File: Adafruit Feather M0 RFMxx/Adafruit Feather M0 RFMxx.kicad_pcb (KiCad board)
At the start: 2 copper layers, 50.8 x 22.9 mm, 50 parts, among them J31 Conn_01x02, J32 Conn_01x02, J33 Conn_01x02, SW1 SPST_TACT-KMR2, U1 2MB Flash, U2 AP2112K-3.3, U3 MCP73831T-2ACI/OT, U31 MCP25625-x-SS, X1 JSTPH, X2 32.768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

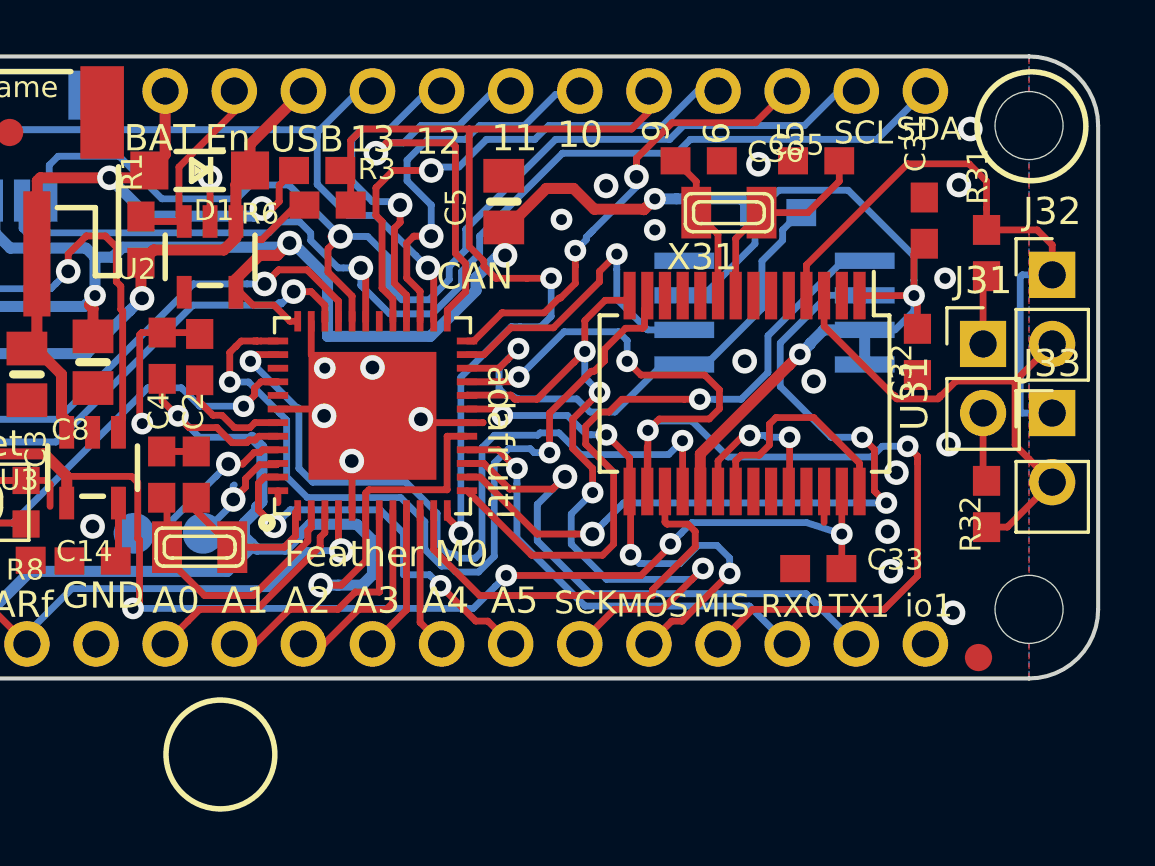
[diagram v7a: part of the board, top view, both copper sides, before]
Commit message: Fix mounting hole. Update silscreen.
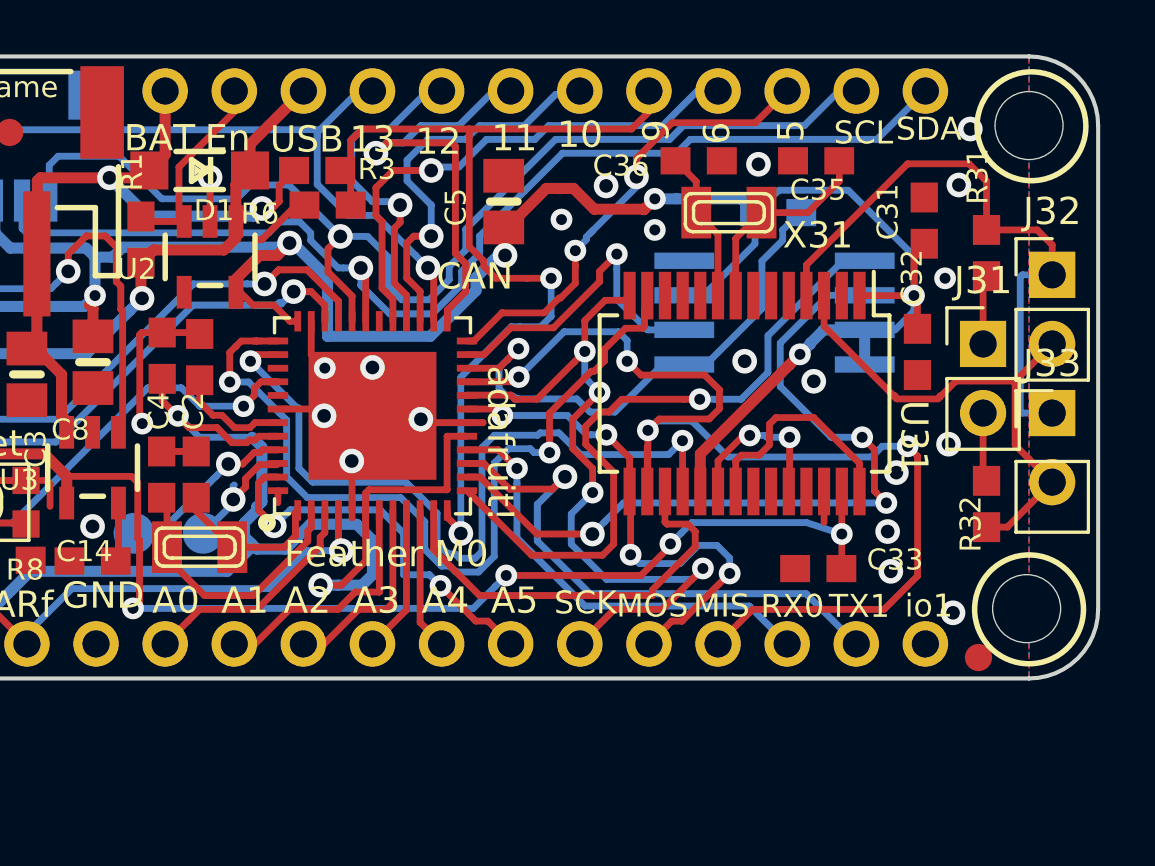
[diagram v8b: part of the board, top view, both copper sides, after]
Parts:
- moved U$31 30.2 mm to (171.4, 113.9)
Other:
- board text added: "ATSAMD21G18 3.3V qwiic and CAN v0.1"
- board text added: "CAN uses: MISO/MOSI/SCK TXD RST, RXD IRQ, 8 CS"
- board text added: "Feather M0 CAN"
- board text added: "H"
- board text removed: "+20dBm"
- board text removed: "ATSAMD21G18 3.3V qwiic and flash v0.1"
- board text removed: "Ant."
- board text removed: "D3"
- board text removed: "D5"
- board text removed: "Feather M0 RFM9x LoRa Radio"
- board text removed: "RF Radio uses: MISO/MOSI/SCK TXD RST, RXD IRQ, 8 CS"
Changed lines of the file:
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@@
   (general
     (thickness 1.6)
-    (drawings 111)
+    (drawings 109)
     (tracks 989)
     (zones 0)
@@
     (35 F.Paste user hide)
     (36 B.SilkS user hide)
-    (37 F.SilkS user)
+    (37 F.SilkS user hide)
     (38 B.Mask user hide)
     (39 F.Mask user hide)
@@
   )
   (module "Adafruit Feather M0 RFMxx:MOUNTINGHOLE_2.5_PLATED" (layer Top)
-    (at 141.6431 119.2276 270)
+    (at 171.3611 113.8936 270)
     (fp_text reference U$31 (at 0 0 270) (layer F.SilkS) hide
       (effects (font (size 1.27 1.27) (thickness 0.15)) (justify right top))
@@
       (effects (font (size 1.27 1.27) (thickness 0.15)) (justify right top))
     )
-    (fp_circle (center 0 0) (end 2 0) (layer F.SilkS) (width 0.2032))
     (fp_circle (center 0 0) (end 1 0) (layer Dwgs.User) (width 2.032))
     (fp_circle (center 0 0) (end 1 0) (layer Dwgs.User) (width 2.032))
     (fp_circle (center 0 0) (end 1 0) (layer Dwgs.User) (width 2.032))
     (fp_circle (center 0 0) (end 1 0) (layer Dwgs.User) (width 2.032))
-    (pad "" np_thru_hole circle (at -5.334 -29.718 270) (size 2.5 2.5) (drill 2.5) (layers *.Cu *.Mask)
+    (fp_circle (center 0 0) (end 2 0) (layer F.SilkS) (width 0.2032))
+    (pad "" np_thru_hole circle (at -0.0254 0.0889 270) (size 2.5 2.5) (drill 2.5) (layers *.Cu *.Mask)
       (solder_mask_margin 0.0508))
   )
@@
   (module "Adafruit Feather M0 RFMxx:0603-NO" (layer Top)
     (at 167.513 99.607 90)
-    (fp_text reference C31 (at 1.778 0.127 90) (layer F.SilkS)
+    (fp_text reference C31 (at -0.723 -0.889 90) (layer F.SilkS)
       (effects (font (size 0.77216 0.77216) (thickness 0.138988)) (justify left bottom))
     )
@@
   (module "Adafruit Feather M0 RFMxx:0603-NO" (layer Top)
     (at 167.259 104.433 270)
-    (fp_text reference C32 (at 1.778 0.127 270) (layer F.SilkS)
+    (fp_text reference C32 (at -1.69 -0.254 270) (layer F.SilkS)
       (effects (font (size 0.77216 0.77216) (thickness 0.138988)) (justify left bottom))
     )
@@
     (tags "SSOP 0.65")
     (attr smd)
-    (fp_text reference U31 (at 0 -6.25 270) (layer F.SilkS)
+    (fp_text reference U31 (at 1.607 -6.227 270 unlocked) (layer F.SilkS)
       (effects (font (size 1 1) (thickness 0.15)))
     )
@@
   (module "Adafruit Feather M0 RFMxx:0603-NO" (layer Top)
     (at 163.537 97.409 180)
-    (fp_text reference C35 (at 1.778 0.127 180) (layer F.SilkS)
+    (fp_text reference C35 (at 0.977 -1.524 180) (layer F.SilkS)
       (effects (font (size 0.77216 0.77216) (thickness 0.138988)) (justify left bottom))
     )
@@
   (module "Adafruit Feather M0 RFMxx:0603-NO" (layer Top)
     (at 159.219 97.409)
-    (fp_text reference C36 (at 1.778 0.127) (layer F.SilkS)
+    (fp_text reference C36 (at -3.898 0.635) (layer F.SilkS)
       (effects (font (size 0.77216 0.77216) (thickness 0.138988)) (justify left bottom))
     )
@@
   (module "Adafruit Feather M0 RFMxx:XTAL3215" (layer Top)
     (at 160.331 99.314)
-    (fp_text reference X31 (at -2.3 2.2) (layer F.SilkS)
-      (effects (font (size 0.9652 0.9652) (thickness 0.077216)) (justify left bottom))
+    (fp_text reference X31 (at 1.975 1.397) (layer F.SilkS)
+      (effects (font (size 0.9652 0.9652) (thickness 0.1524)) (justify left bottom))
     )
     (fp_text value XTAL-3.2X1.5 (at -2.6 -1.2) (layer F.Fab)
@@
     (effects (font (size 0.9652 0.9652) (thickness 0.1524)) (justify mirror))
   )
-  (gr_text "Feather M0\nRFM9x LoRa Radio" (at 145.3261 100.1776) (layer B.SilkS)
+  (gr_text "Feather M0\nCAN" (at 145.3261 100.1776) (layer B.SilkS)
     (effects (font (size 1.2065 1.2065) (thickness 0.1651)) (justify mirror))
   )
-  (gr_text "ATSAMD21G18 3.3V\nqwiic and flash v0.1" (at 145.288 103.505) (layer B.SilkS)
+  (gr_text "ATSAMD21G18 3.3V\nqwiic and CAN v0.1" (at 145.288 103.505) (layer B.SilkS)
     (effects (font (size 0.9652 0.9652) (thickness 0.1524)) (justify mirror))
   )
@@
     (effects (font (size 0.9652 0.9652) (thickness 0.1524)) (justify right top mirror))
   )
-  (gr_text D3 (at 171.069 100.203 -90) (layer B.SilkS)
+  (gr_text H (at 171.069 100.203 -90) (layer B.SilkS)
     (effects (font (size 0.9652 0.9652) (thickness 0.1524)) (justify right top mirror))
   )
-  (gr_text D5 (at 171.1071 102.743 -90) (layer B.SilkS)
-    (effects (font (size 0.9652 0.9652) (thickness 0.1524)) (justify right top mirror))
-  )
-  (gr_text "RF Radio uses:\nMISO/MOSI/SCK\nTXD RST, RXD IRQ, 8 CS" (at 145.669 107.061) (layer B.SilkS)
+  (gr_text "CAN uses:\nMISO/MOSI/SCK\nTXD RST, RXD IRQ, 8 CS" (at 145.669 107.061) (layer B.SilkS)
     (effects (font (size 0.8128 0.8128) (thickness 0.1524)) (justify mirror))
   )
@@
     (effects (font (size 1.08585 1.08585) (thickness 0.16002)) (justify left bottom mirror))
   )
-  (gr_text Ant. (at 172.2501 110.0201 -90) (layer B.SilkS)
+  (gr_text H (at 170.18 106.807 -90) (layer B.SilkS)
     (effects (font (size 1.08585 1.08585) (thickness 0.16002)) (justify left bottom mirror))
   )
-  (gr_text +20dBm (at 170.5991 112.0521 -90) (layer B.SilkS)
-    (effects (font (size 1.08585 1.08585) (thickness 0.16002)) (justify left bottom mirror))
-  )
